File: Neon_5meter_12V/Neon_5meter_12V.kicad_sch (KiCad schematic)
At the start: 48 parts, among them J1 Conn_01x16_Pin, J2 Barrel_Jack_MountingPin, J3 Conn_01x16_Pin, J4 Barrel_Jack_MountingPin, J5 Barrel_Jack_MountingPin, J6 Conn_01x03_Pin, Q1 IRLML2502TRPBF, Q2 IRLML2502TRPBF, Q3 BSS138, Q4 BSS138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

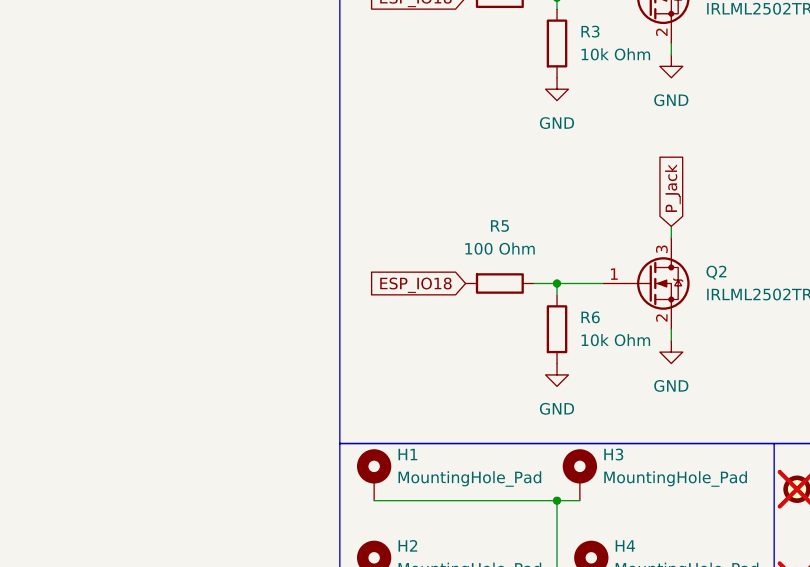
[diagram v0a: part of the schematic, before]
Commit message: updated component placement
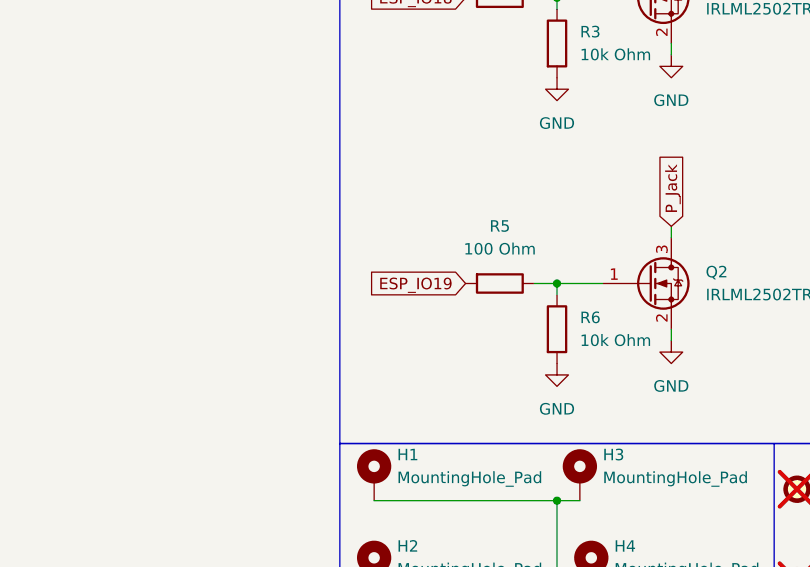
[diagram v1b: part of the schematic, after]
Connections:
- net ESP_IO18: no longer R5.2
- net ESP_IO19: now also R5.2
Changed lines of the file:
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@@
 		)
 	)
-	(global_label "ESP_IO18"
+	(global_label "ESP_IO19"
 		(shape input)
 		(at 26.67 156.21 180)

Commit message: updated 1x3 pin header jst connector footprint
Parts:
- J6: footprint Connector_PinHeader_2.54mm:PinHeader_1x03_P2.54mm_Horizontal -> Connector_PinHeader_2.54mm:PinHeader_1x03_P2.54mm_Vertical
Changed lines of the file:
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@@
 			)
 		)
-		(property "Footprint" "Connector_PinHeader_2.54mm:PinHeader_1x03_P2.54mm_Horizontal"
+		(property "Footprint" "Connector_PinHeader_2.54mm:PinHeader_1x03_P2.54mm_Vertical"
 			(at 195.58 30.48 0)
 			(effects

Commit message: updated placement removed pinheaders
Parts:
- J1, J3: now not fitted; now left out of the parts list
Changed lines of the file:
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@@
 		(unit 1)
 		(exclude_from_sim no)
-		(in_bom yes)
-		(on_board yes)
-		(dnp no)
+		(in_bom no)
+		(on_board no)
+		(dnp yes)
 		(fields_autoplaced yes)
 		(property "Reference" "J3"
@@
 		(unit 1)
 		(exclude_from_sim no)
-		(in_bom yes)
-		(on_board yes)
-		(dnp no)
+		(in_bom no)
+		(on_board no)
+		(dnp yes)
 		(property "Reference" "J1"
 			(at 248.285 111.76 0)

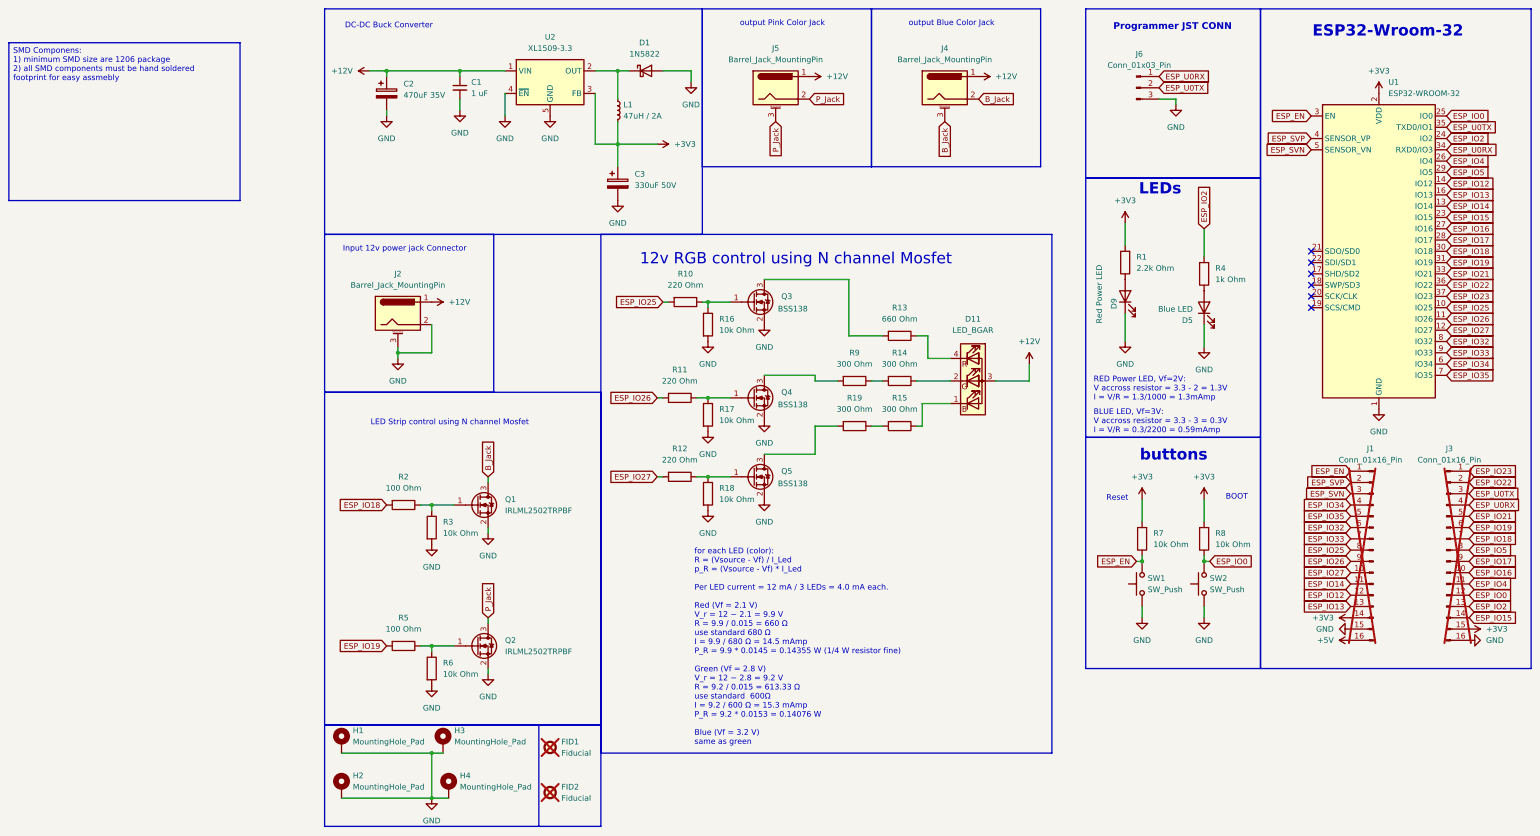
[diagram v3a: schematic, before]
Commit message: updated tutankhamon logo
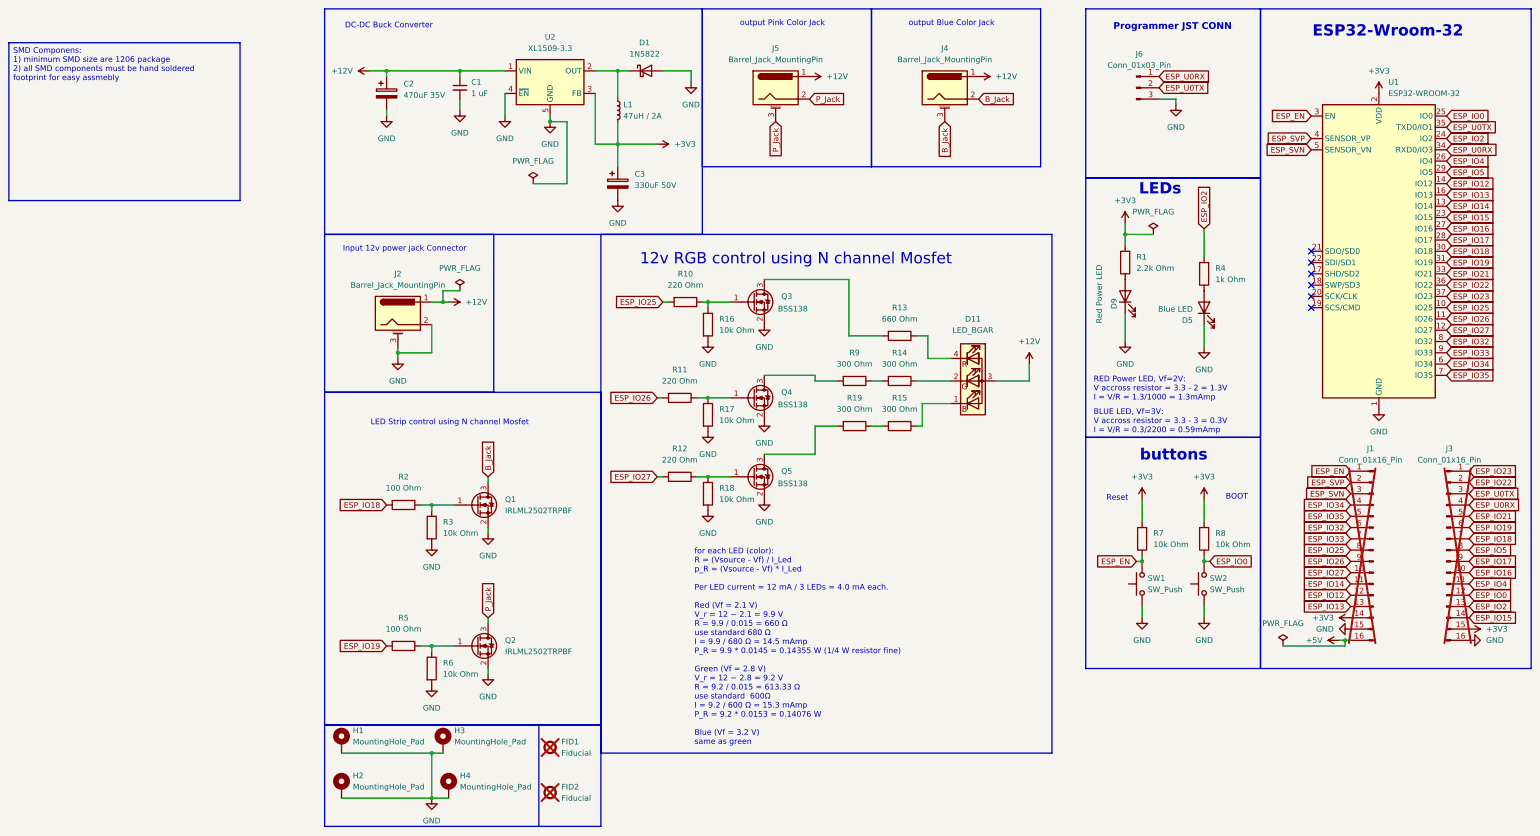
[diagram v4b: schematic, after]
